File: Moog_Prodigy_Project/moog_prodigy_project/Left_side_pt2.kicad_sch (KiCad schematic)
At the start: 97 parts, among them Q1 CA3046, Q11 BC107, Q13 BF244A, Q16 BF244A, Q17 BC549, Q2 CA3046, SW3 SW_Slide_DPDT, U10 AD8066ARM, U22 +12V, U23 +12V, U24 +12V, U25 +12V, U26 +12V, U27 +12V, U28 +12V, U29 +12V, U2B1 OPA134, U30 +12V, U31 +12V, U32 +12V, U33 +12V, U42 +12V, U43 -12V, U44 -12V, U45 -12V, U46 -12V, U47 -12V, U48 -12V, U49 -12V, U4B OPA134, U50 -12V, U51 -12V, U52 -12V, U53 +12V, U54 -12V, U8 NE5532, U9 LM393BIPWR

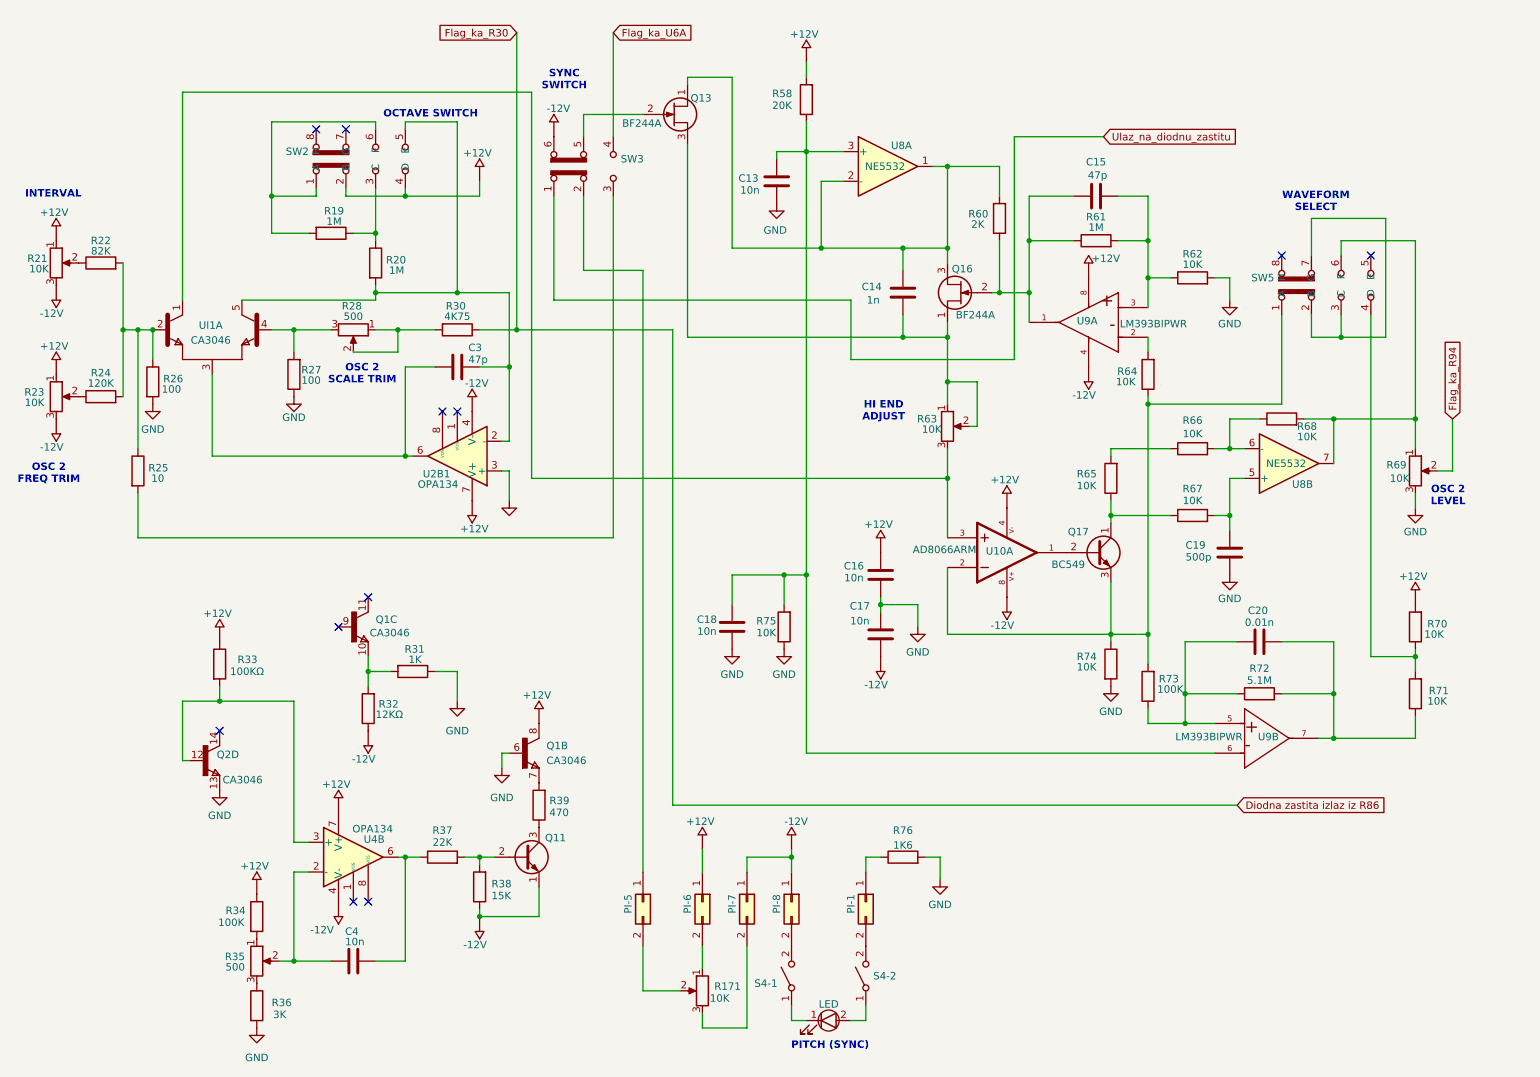
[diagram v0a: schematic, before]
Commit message: Vcc fix, banana jack, connector, OP adding top sch
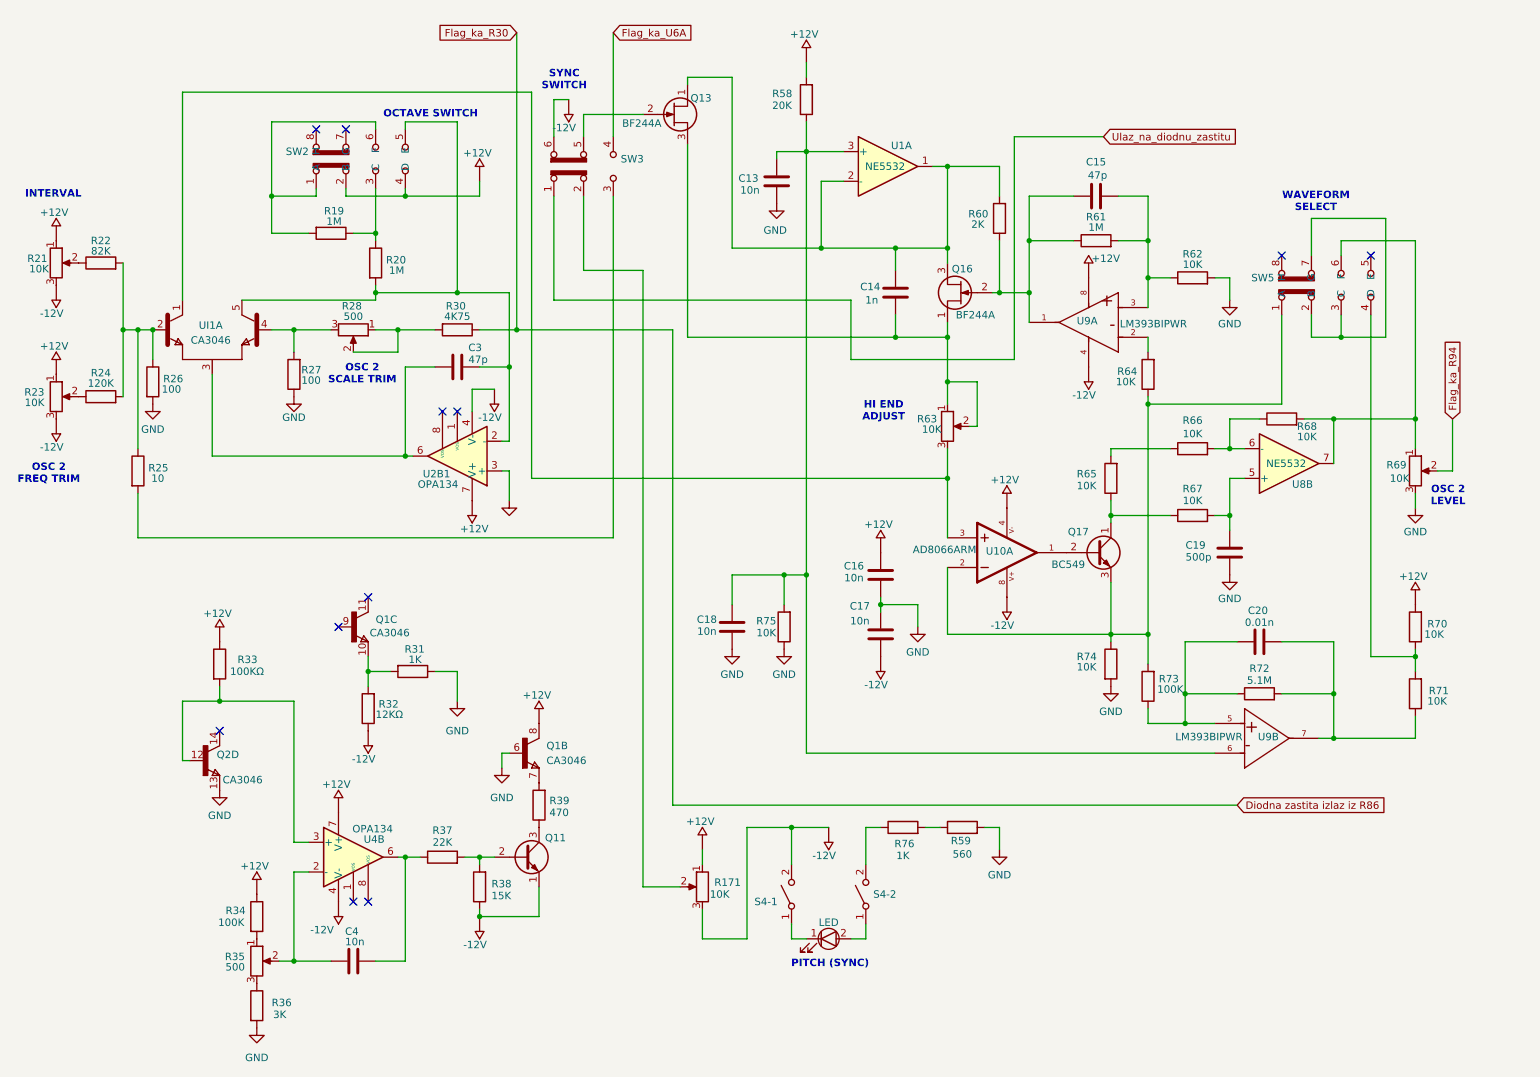
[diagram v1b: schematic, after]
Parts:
- removed PI-1, PI-5, PI-6, PI-7, PI-8: Conn_02x01, symbol Connector_Generic:Conn_02x01
- added R59: 560, symbol Device:R
- R76: value 1K6 -> 1K
- renumbered U8 to U1
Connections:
- net GND: now also R59.2; no longer R76.2
- net at U54.: now also R171.3, S4-1.2 (B)
- net at U29.: now also R171.1
- net at S4-2.2 (B): now also R76.1
- net at SW3.2 (B): now also R171.2
- new net: R59.1, R76.2
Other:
- moved on the sheet: C14, LED, R171, R76, S4-1, S4-2

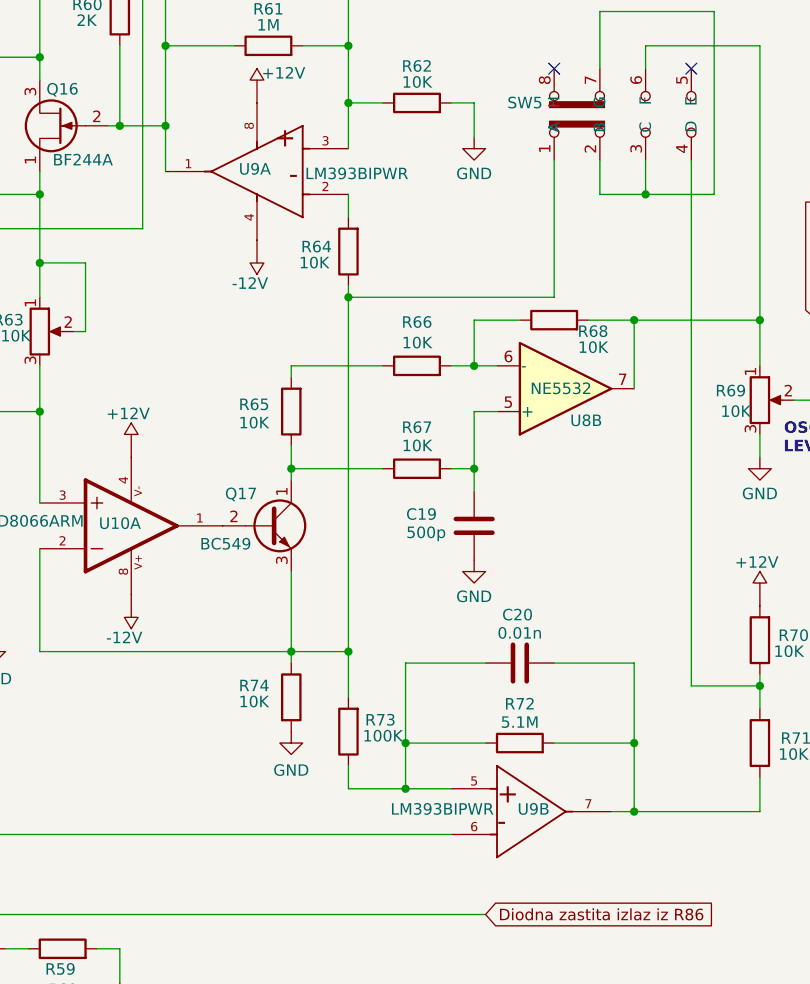
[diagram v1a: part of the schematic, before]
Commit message: 4007 update, impor biblioteka LM 393
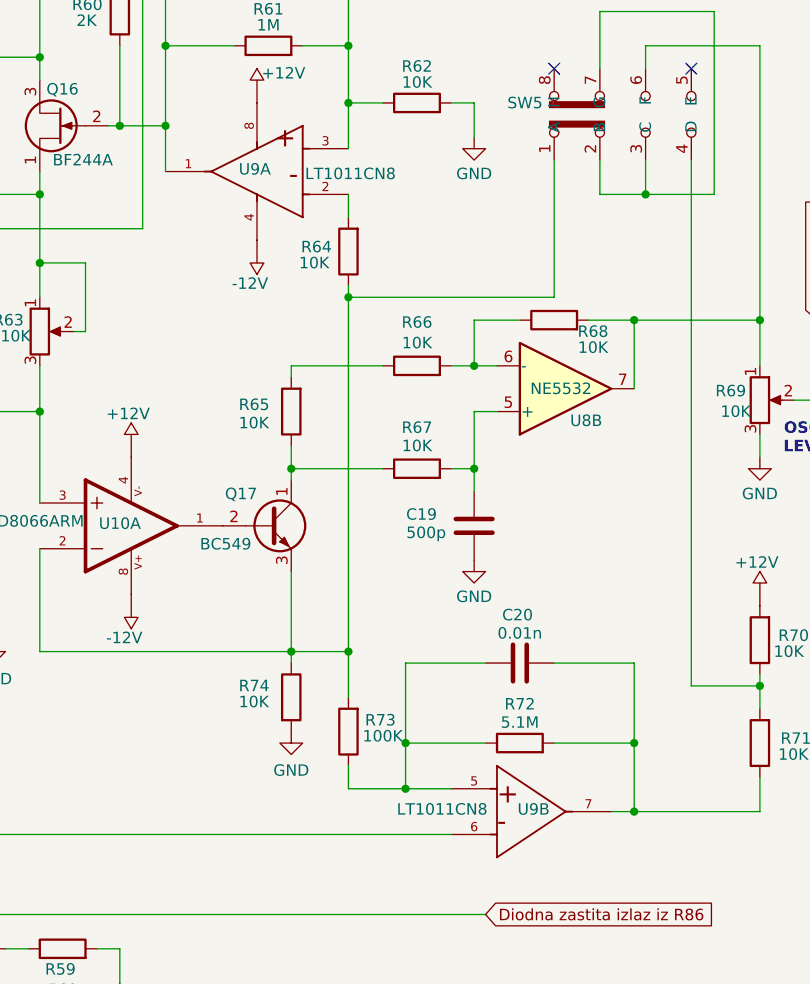
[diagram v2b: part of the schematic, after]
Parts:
- U9: value LM393BIPWR -> LT1011CN8; footprint (none) -> Package_DIP:DIP-8_W7.62mm_Socket
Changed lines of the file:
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@@
 			)
 		)
-		(property "Value" "LM393BIPWR"
+		(property "Value" "LT1011CN8"
 			(at 200.914 66.294 0)
 			(effects
@@
 			)
 		)
-		(property "Footprint" ""
+		(property "Footprint" "Package_DIP:DIP-8_W7.62mm_Socket"
 			(at 205.74 63.5 0)
 			(effects
@@
 			)
 		)
-		(property "Value" "LM393BIPWR"
+		(property "Value" "LT1011CN8"
 			(at 216.154 136.906 0)
 			(effects
@@
 			)
 		)
-		(property "Footprint" ""
+		(property "Footprint" "Package_DIP:DIP-8_W7.62mm_Socket"
 			(at 217.17 134.62 0)
 			(effects

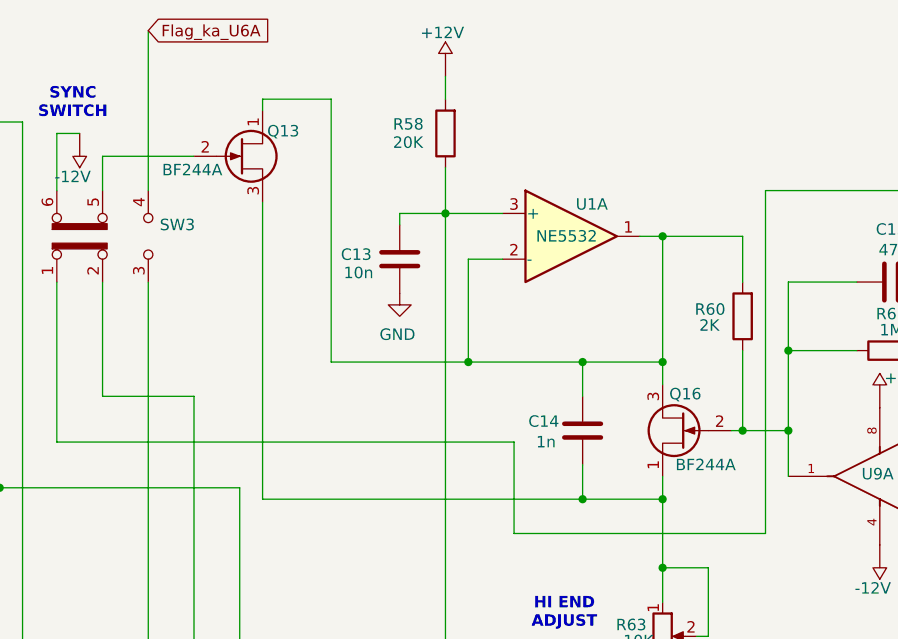
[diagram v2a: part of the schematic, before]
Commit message: Zamena fet-ova E112 sa BF256C + update dokumentacije
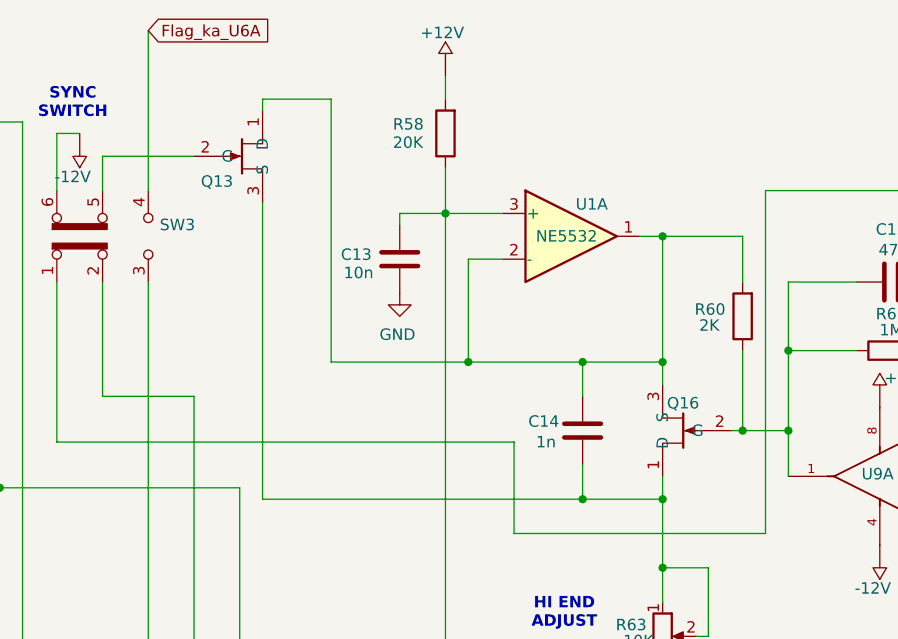
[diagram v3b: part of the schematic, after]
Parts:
- removed Q13, Q16: BF244A, Package_TO_SOT_THT:TO-92_Inline, symbol Transistor_FET:BF244A
- added Q13, Q16: ~, BF256C:TO92127P478H483-3, symbol Transistor_FET:BF256C
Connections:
- net at C15.1, R60.1, R61.1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: now also Q16.2 (G)
- net at C14.1, R63.1, R63.2: now also Q13.3 (S), Q16.1 (D)
- net at C14.2, R60.2, U1.1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: now also Q13.1 (D), Q16.3 (S)
- net at SW3.5 (B): now also Q13.2 (G)
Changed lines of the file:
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@@
 	)
 	(symbol
+		(lib_id "Transistor_FET:BF256C")
+		(at 176.53 58.42 180)
+		(unit 1)
+		(exclude_from_sim no)
+		(in_bom yes)
+		(on_board yes)
+		(dnp no)
+		(property "Reference" "Q16"
+			(at 175.514 57.912 0)
+			(effects
+				(font
+					(size 1.27 1.27)
+				)
+				(justify left)
+			)
+		)
+		(property "Value" "~"
+			(at 170.18 62.2299 0)
+			(effects
+				(font
+					(size 1.27 1.27)
+				)
+				(justify left)
+				(hide yes)
+			)
+		)
+		(property "Footprint" "BF256C:TO92127P478H483-3"
+			(at 176.53 58.42 0)
+			(effects
+				(font
+					(size 1.27 1.27)
+				)
+				(hide yes)
+			)
+		)
+		(property "Datasheet" ""
+			(at 176.53 58.42 0)
+			(effects
+				(font
+					(size 1.27 1.27)
+				)
+				(hide yes)
+			)
+		)
+		(property "Description" ""
+			(at 176.53 58.42 0)
+			(effects
+				(font
+					(size 1.27 1.27)
+				)
+				(hide yes)
+			)
+		)
+		(pin "3"
+		)
+		(pin "1"
+		)
+		(pin "2"
+		)
+		(instances
+			(project "moog_prodigy_project"
+				(path "/db469bdb-b6c3-4a16-9199-d4e6b8d556e8/4ed67b3d-2561-481b-964c-8f7d9fc9a038"
+					(reference "Q16")
+					(unit 1)
+				)
+			)
+		)
+	)
+	(symbol
 		(lib_id "Device:R")
 		(at 87.63 67.31 270)
@@
 	)
 	(symbol
-		(lib_id "Transistor_FET:BF244A")
-		(at 124.46 30.48 0)
+		(lib_id "Amplifier_Operational:NE5532")
+		(at 161.29 39.37 0)
 		(unit 1)
 		(exclude_from_sim no)
@@
 		(on_board yes)
 		(dnp no)
-		(property "Reference" "Q13"
-			(at 127.508 27.686 0)
+		(property "Reference" "U1"
+			(at 163.576 35.814 0)
 			(effects
 				(font
 					(size 1.27 1.27)
 				)
-				(justify left)
 			)
 		)
-		(property "Value" "BF244A"
-			(at 115.824 32.004 0)
+		(property "Value" "NE5532"
+			(at 160.782 39.37 0)
 			(effects
 				(font
 					(size 1.27 1.27)
 				)
-				(justify left)
 			)
 		)
-		(property "Footprint" "Package_TO_SOT_THT:TO-92_Inline"
-			(at 129.54 32.385 0)
+		(property "Footprint" ""
+			(at 161.29 39.37 0)
 			(effects
 				(font
 					(size 1.27 1.27)
-					(italic yes)
 				)
-				(justify left)
 				(hide yes)
 			)
 		)
-		(property "Datasheet" "https://media.digikey.com/pdf/Data%20Sheets/Fairchild%20PDFs/BF244x.pdf"
-			(at 129.54 34.29 0)
+		(property "Datasheet" "http://www.ti.com/lit/ds/symlink/ne5532.pdf"
+			(at 161.29 39.37 0)
 			(effects
 				(font
 					(size 1.27 1.27)
 				)
-				(justify left)
 				(hide yes)
 			)
 		)
-		(property "Description" "50mA Id, 30V Vgs, N-Channel FET Transistor, TO-92"
-			(at 124.46 30.48 0)
+		(property "Description" "Dual Low-Noise Operational Amplifiers, DIP-8/SOIC-8"
+			(at 161.29 39.37 0)
 			(effects
 				(font
@@
 			)
 		)
-		(pin "2"
+		(pin "6"
 		)
 		(pin "1"
 		)
+		(pin "2"
+		)
 		(pin "3"
 		)
+		(pin "5"
+		)
+		(pin "7"
+		)
+		(pin "4"
+		)
+		(pin "8"
+		)
 		(instances
-			(project ""
-				(path "/d7ecab91-fc93-47c1-809d-3a7b4e998ed7"
-					(reference "Q13")
-					(unit 1)
-				)
-			)
 			(project "moog_prodigy_project"
 				(path "/db469bdb-b6c3-4a16-9199-d4e6b8d556e8/4ed67b3d-2561-481b-964c-8f7d9fc9a038"
-					(reference "Q13")
+					(reference "U1")
 					(unit 1)
 				)
@@
 	)
 	(symbol
-		(lib_id "Amplifier_Operational:NE5532")
-		(at 161.29 39.37 0)
+		(lib_id "Transistor_FET:BF256C")
+		(at 121.92 33.02 0)
 		(unit 1)
 		(exclude_from_sim no)
@@
 		(on_board yes)
 		(dnp no)
-		(property "Reference" "U1"
-			(at 163.576 35.814 0)
+		(property "Reference" "Q13"
+			(at 120.142 33.274 0)
 			(effects
 				(font
 					(size 1.27 1.27)
 				)
+				(justify left)
 			)
 		)
-		(property "Value" "NE5532"
-			(at 160.782 39.37 0)
+		(property "Value" "~"
+			(at 128.27 29.2101 0)
 			(effects
 				(font
 					(size 1.27 1.27)
 				)
+				(justify left)
+				(hide yes)
 			)
 		)
-		(property "Footprint" ""
-			(at 161.29 39.37 0)
+		(property "Footprint" "BF256C:TO92127P478H483-3"
+			(at 121.92 33.02 0)
 			(effects
 				(font
@@
 			)
 		)
-		(property "Datasheet" "http://www.ti.com/lit/ds/symlink/ne5532.pdf"
-			(at 161.29 39.37 0)
+		(property "Datasheet" ""
+			(at 121.92 33.02 0)
 			(effects
 				(font
@@
 			)
 		)
-		(property "Description" "Dual Low-Noise Operational Amplifiers, DIP-8/SOIC-8"
-			(at 161.29 39.37 0)
+		(property "Description" ""
+			(at 121.92 33.02 0)
 			(effects
 				(font
@@
 			)
 		)
-		(pin "6"
+		(pin "3"
 		)
 		(pin "1"
@@
 		(pin "2"
 		)
-		(pin "3"
-		)
-		(pin "5"
-		)
-		(pin "7"
-		)
-		(pin "4"
-		)
-		(pin "8"
-		)
 		(instances
 			(project "moog_prodigy_project"
 				(path "/db469bdb-b6c3-4a16-9199-d4e6b8d556e8/4ed67b3d-2561-481b-964c-8f7d9fc9a038"
-					(reference "U1")
+					(reference "Q13")
 					(unit 1)
 				)
@@
 					(unit 1)
 				)
-			)
-		)
-	)
-	(symbol
-		(lib_id "Transistor_FET:BF244A")
-		(at 173.99 60.96 180)
-		(unit 1)
-		(exclude_from_sim no)
-		(in_bom yes)
-		(on_board yes)
-		(dnp no)
-		(property "Reference" "Q16"
-			(at 175.768 56.896 0)
-			(effects
-				(font
-					(size 1.27 1.27)
-				)
-				(justify left)
-			)
-		)
-		(property "Value" "BF244A"
-			(at 179.578 64.77 0)
-			(effects
-				(font
-					(size 1.27 1.27)
-				)
-				(justify left)
-			)
-		)
-		(property "Footprint" "Package_TO_SOT_THT:TO-92_Inline"
-			(at 168.91 59.055 0)
-			(effects
-				(font
-					(size 1.27 1.27)
-					(italic yes)
-				)
-				(justify left)
-				(hide yes)
-			)
-		)
-		(property "Datasheet" "https://media.digikey.com/pdf/Data%20Sheets/Fairchild%20PDFs/BF244x.pdf"
-			(at 168.91 57.15 0)
-			(effects
-				(font
-					(size 1.27 1.27)
-				)
-				(justify left)
-				(hide yes)
-			)
-		)
-		(property "Description" "50mA Id, 30V Vgs, N-Channel FET Transistor, TO-92"
-			(at 173.99 60.96 0)
-			(effects
-				(font
-					(size 1.27 1.27)
-				)
-				(hide yes)
-			)
-		)
-		(pin "2"
-		)
-		(pin "1"
-		)
-		(pin "3"
-		)
-		(instances
-			(project "Left_side_pt2"
-				(path "/d7ecab91-fc93-47c1-809d-3a7b4e998ed7"
-					(reference "Q16")
-					(unit 1)
-				)
-			)
-			(project "moog_prodigy_project"
-				(path "/db469bdb-b6c3-4a16-9199-d4e6b8d556e8/4ed67b3d-2561-481b-964c-8f7d9fc9a038"
-					(reference "Q16")
-					(unit 1)
-				)

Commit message: New update footprints
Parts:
- renumbered LED to LED1, U4B to U4B1, U1 to U8, UI1 to UI3

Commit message: Footpring fix 2
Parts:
- UI3: footprint (none) -> CA3046:DIL14
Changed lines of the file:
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@@
 			)
 		)
-		(property "Footprint" ""
+		(property "Footprint" "CA3046:DIL14"
 			(at 45.72 67.31 0)
 			(effects
